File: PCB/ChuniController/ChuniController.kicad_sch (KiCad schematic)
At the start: 2 parts, among them U1 MPR121QR2_BOARD

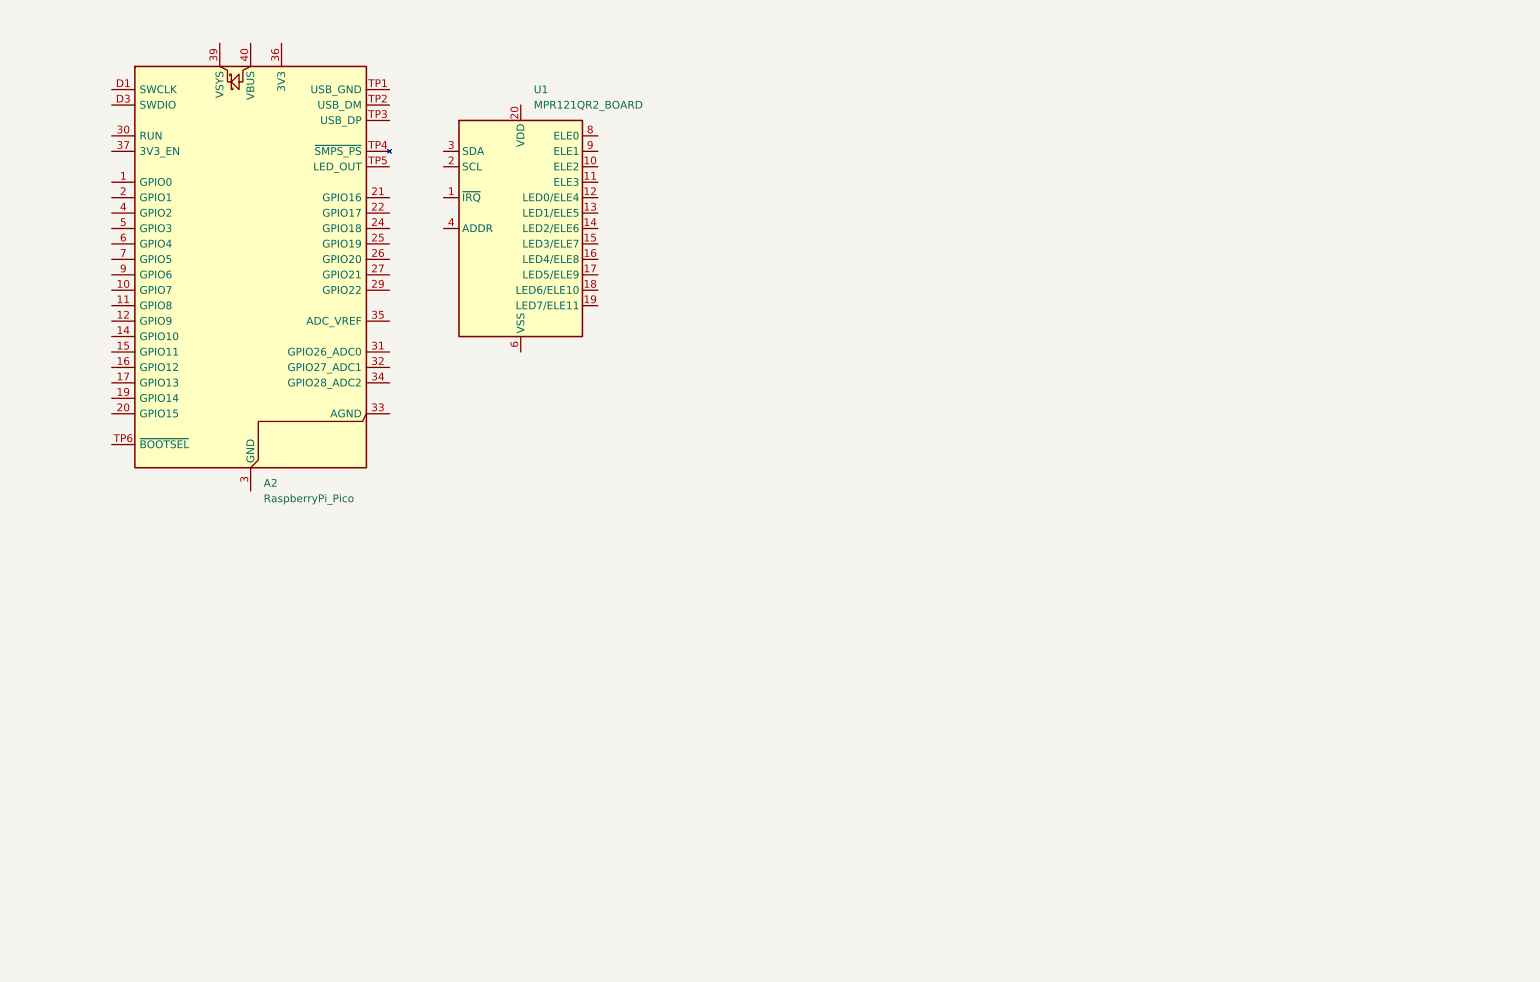
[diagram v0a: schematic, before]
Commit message: Add touch sensor
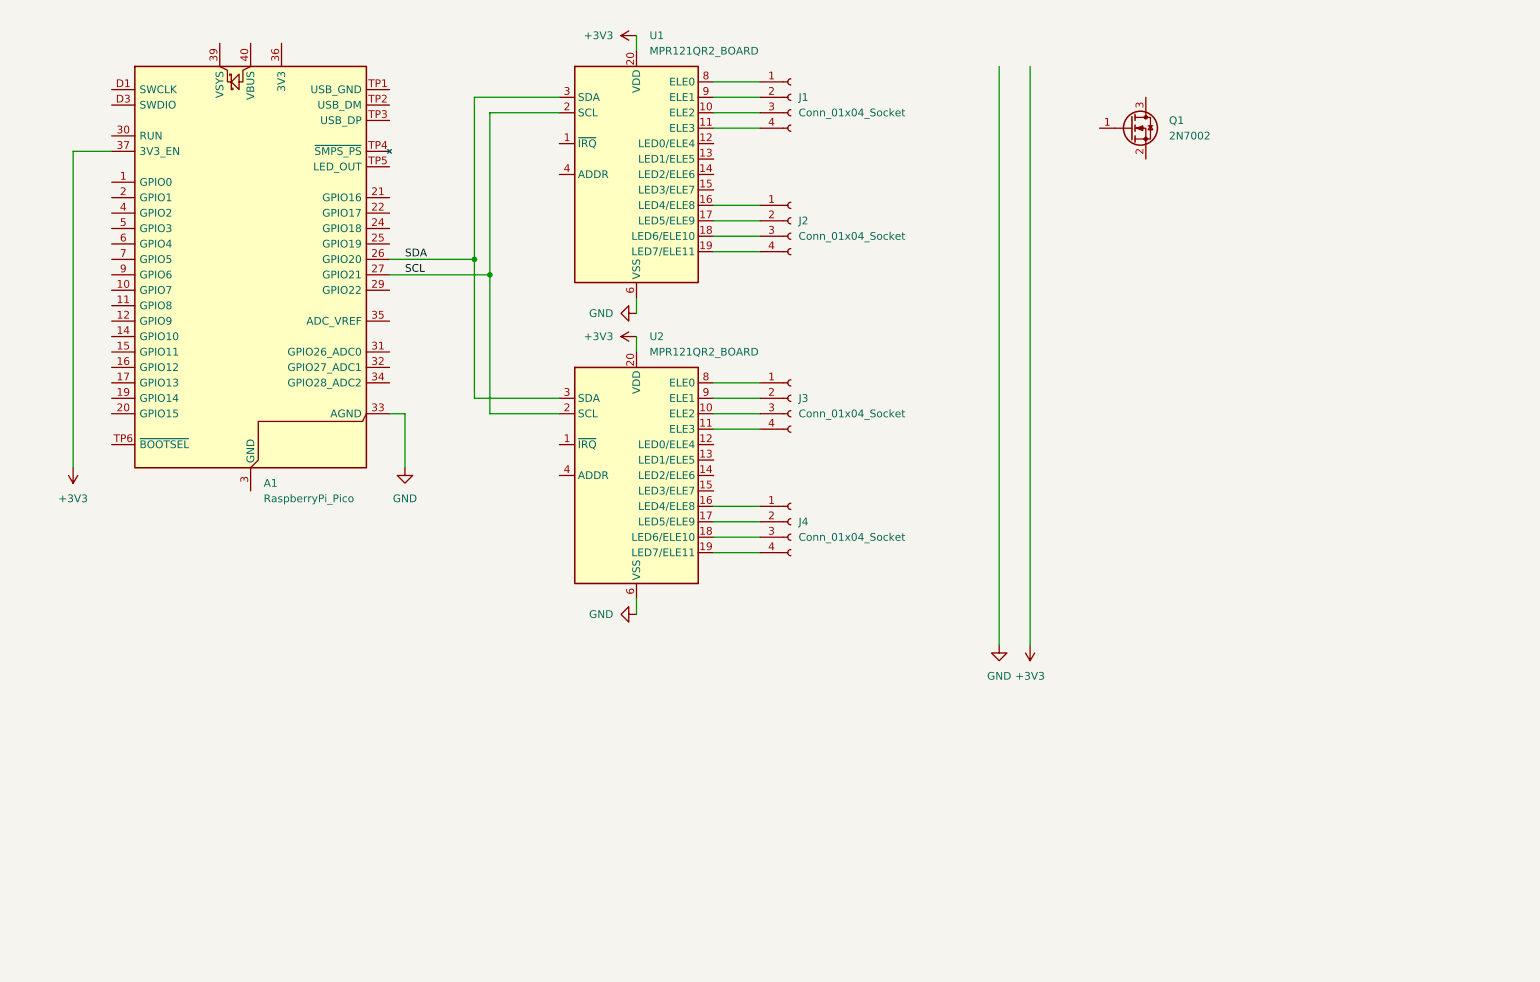
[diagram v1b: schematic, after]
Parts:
- added J1, J2, J3, J4: Conn_01x04_Socket, symbol Connector:Conn_01x04_Socket
- added Q1: 2N7002, Package_TO_SOT_SMD:SOT-23, symbol Transistor_FET:2N7002
- added U2: MPR121QR2_BOARD, chu_main:MPR121_BOARD, symbol 2025-07-05_08-37-47:MPR121QR2_BOARD
- renumbered A2 to A1
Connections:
- net SDA: now reaches A1.26 (GPIO20)
- net SDA: now also U1.3 (SDA), U2.3 (SDA)
- net SCL: now reaches A1.27 (GPIO21)
- net SCL: now also U1.2 (SCL), U2.2 (SCL)
- net GND: now reaches A1.33 (AGND)
- net GND: now also U1.6 (VSS), U2.6 (VSS)
- net +3V3: now reaches A1.37 (3V3_EN)
- net +3V3: now also U1.20 (VDD), U2.20 (VDD)
- net at U1.10 (ELE2): now also J1.3 (Pin_3)
- net at U1.11 (ELE3): now also J1.4 (Pin_4)
- net at U1.16 (LED4/ELE8): now also J2.1 (Pin_1)
- net at U1.17 (LED5/ELE9): now also J2.2 (Pin_2)
- net at U1.18 (LED6/ELE10): now also J2.3 (Pin_3)
- net at U1.19 (LED7/ELE11): now also J2.4 (Pin_4)
- net at U1.8 (ELE0): now also J1.1 (Pin_1)
- net at U1.9 (ELE1): now also J1.2 (Pin_2)
- new net: J4.1 (Pin_1), U2.16 (LED4/ELE8)
- new net: J4.2 (Pin_2), U2.17 (LED5/ELE9)
- new net: J4.3 (Pin_3), U2.18 (LED6/ELE10)
- new net: J4.4 (Pin_4), U2.19 (LED7/ELE11)
- new net: J3.3 (Pin_3), U2.10 (ELE2)
- new net: J3.4 (Pin_4), U2.11 (ELE3)
- new net: J3.1 (Pin_1), U2.8 (ELE0)
- new net: J3.2 (Pin_2), U2.9 (ELE1)
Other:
- moved on the sheet: U1

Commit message: Add IR sensor
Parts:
- added D1, D2, D3, D4, D5, D6: IR333C-A, LED_THT:LED_D5.0mm, symbol Device:LED
- added Q10, Q11, Q12, Q4, Q6: 2N7002, Package_TO_SOT_SMD:SOT-23, symbol Transistor_FET:2N7002
- added Q2, Q3, Q5, Q7, Q8, Q9: PT333-3B, OptoDevice:Kingbright_KPS-3227, symbol Sensor_Optical:BP103B
- added R1, R16, R17, R18, R6, R9: 1R, symbol Device:R
- added R10, R12, R14, R2, R4, R7: 10R, symbol Device:R
- added R11, R13, R15, R3, R5, R8: 10K, symbol Device:R
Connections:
- net +3V3: now also D1.2 (A), D2.2 (A), D3.2 (A), D4.2 (A), D5.2 (A), D6.2 (A), Q2.1 (C), Q3.1 (C), Q5.1 (C), Q7.1 (C), Q8.1 (C), Q9.1 (C)
- net GND: now also Q1.2 (S), Q10.2 (S), Q11.2 (S), Q12.2 (S), Q4.2 (S), Q6.2 (S), R11.1, R13.1, R15.1, R3.1, R5.1, R8.1
- net at Q1.1 (G): now also R2.2
- net at Q1.3 (D): now also R1.2
- new net: Q11.1 (G), R12.2
- new net: Q10.1 (G), R10.2
- new net: Q6.1 (G), R7.2
- new net: D1.1 (K), R1.1
- new net: D6.1 (K), R18.1
- new net: Q12.3 (D), R18.2
- new net: D3.1 (K), R9.1
- new net: D2.1 (K), R6.1
- new net: Q7.2 (E), R11.2
- new net: Q6.3 (D), R9.2
- new net: Q8.2 (E), R13.2
- new net: Q9.2 (E), R15.2
- new net: D4.1 (K), R16.1
- new net: Q11.3 (D), R17.2
- new net: Q10.3 (D), R16.2
- new net: Q5.2 (E), R8.2
- new net: Q2.2 (E), R3.2
- new net: Q4.1 (G), R4.2
- new net: Q3.2 (E), R5.2
- new net: Q4.3 (D), R6.2
- new net: Q12.1 (G), R14.2
- new net: D5.1 (K), R17.1
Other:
- moved on the sheet: Q1

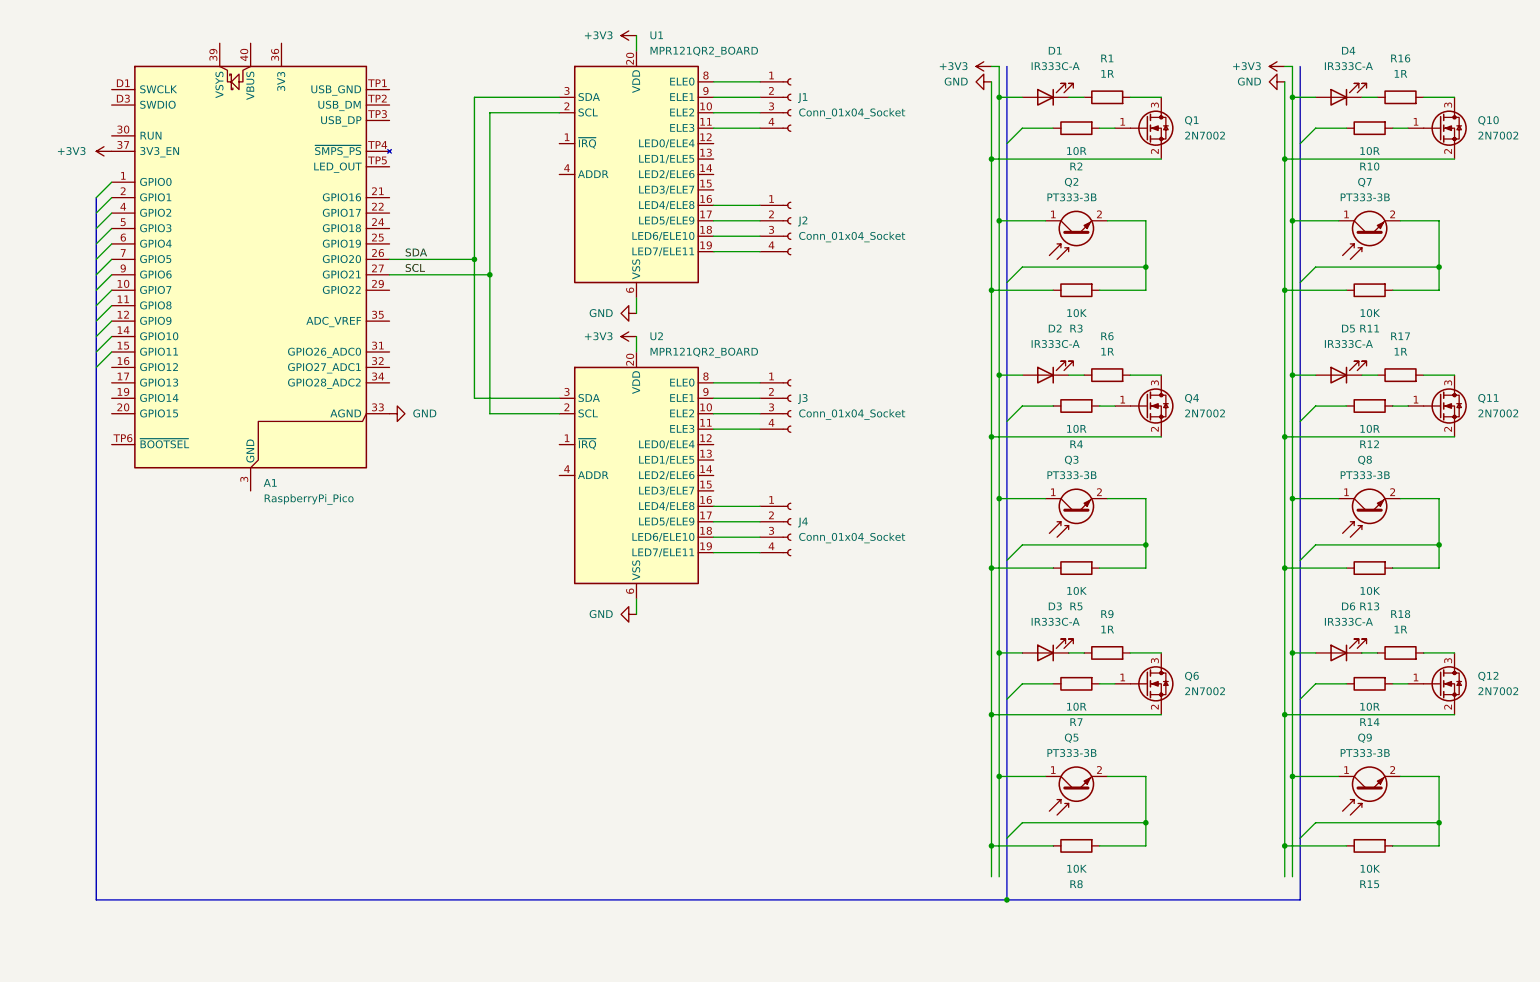
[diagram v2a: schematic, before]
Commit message: Seperate schematic to multiple page
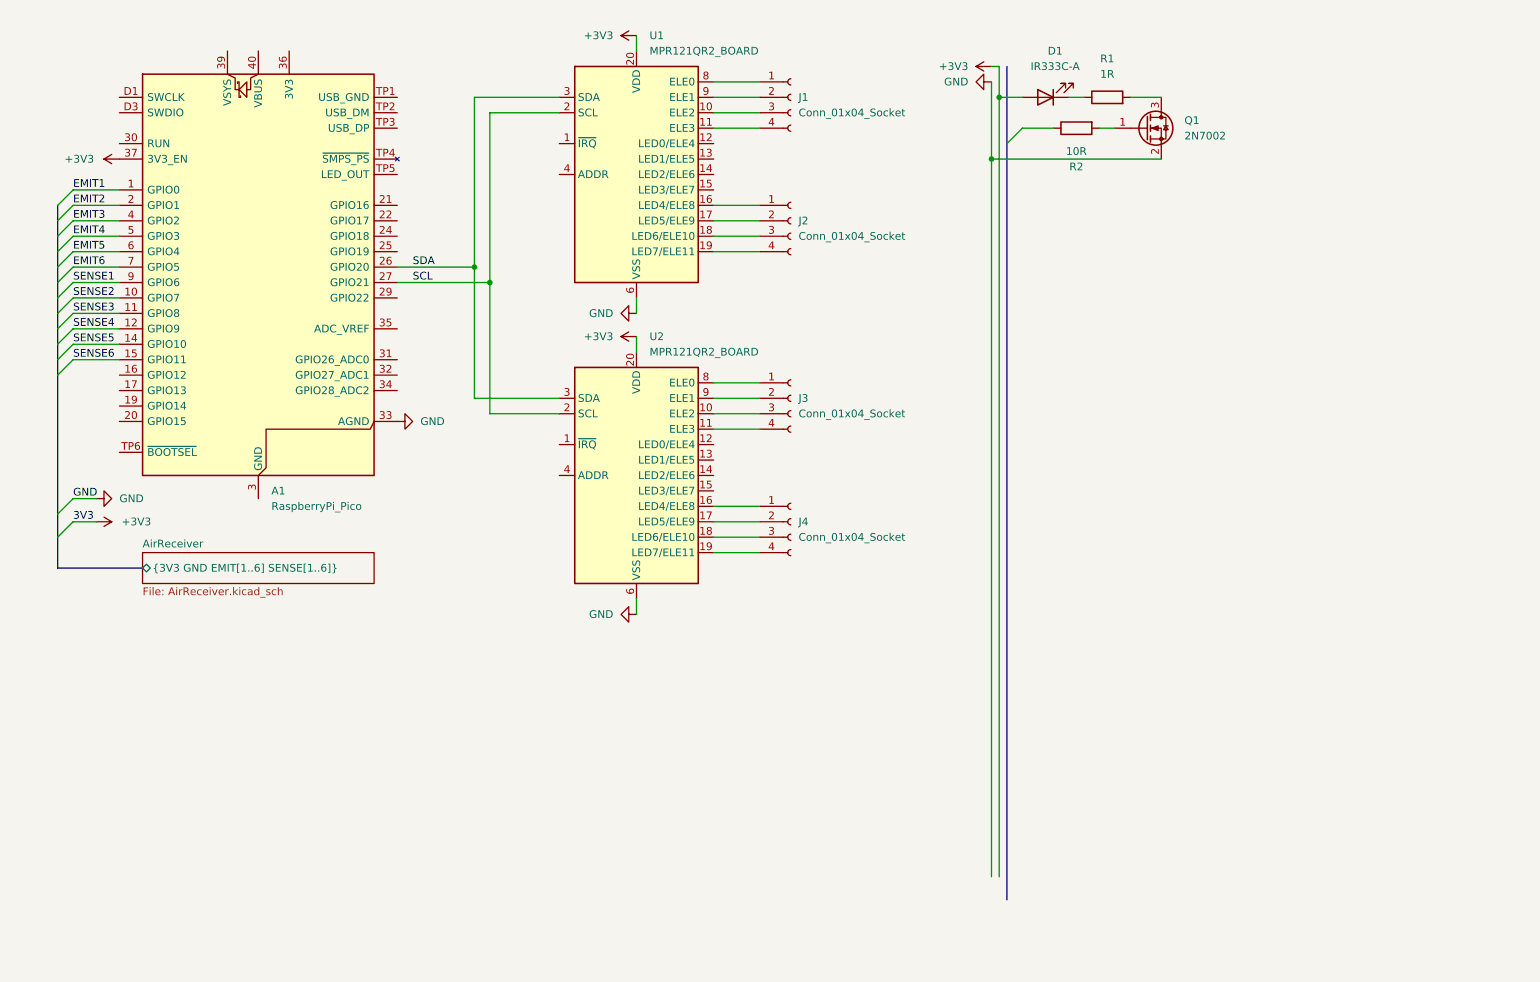
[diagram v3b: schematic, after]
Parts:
- removed D2, D3, D4, D5, D6: IR333C-A, LED_THT:LED_D5.0mm, symbol Device:LED
- removed Q10, Q11, Q12, Q4, Q6: 2N7002, Package_TO_SOT_SMD:SOT-23, symbol Transistor_FET:2N7002
- removed Q2, Q3, Q5, Q7, Q8, Q9: PT333-3B, OptoDevice:Kingbright_KPS-3227, symbol Sensor_Optical:BP103B
- removed R10, R12, R14, R4, R7: 10R, symbol Device:R
- removed R11, R13, R15, R3, R5, R8: 10K, symbol Device:R
- removed R16, R17, R18, R6, R9: 1R, symbol Device:R
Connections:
- net EMIT1: now reaches A1.1 (GPIO0)
- net SENSE2: now reaches A1.10 (GPIO7)
- net SENSE3: now reaches A1.11 (GPIO8)
- net SENSE4: now reaches A1.12 (GPIO9)
- net SENSE5: now reaches A1.14 (GPIO10)
- net SENSE6: now reaches A1.15 (GPIO11)
- net EMIT2: now reaches A1.2 (GPIO1)
- net EMIT3: now reaches A1.4 (GPIO2)
- net EMIT4: now reaches A1.5 (GPIO3)
- net EMIT5: now reaches A1.6 (GPIO4)
- net EMIT6: now reaches A1.7 (GPIO5)
- net SENSE1: now reaches A1.9 (GPIO6)
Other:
- added sheet AirReceiver (AirReceiver.kicad_sch)
- moved on the sheet: A1

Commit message: PCB + CAD
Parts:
- removed D1: IR333C-A, LED_THT:LED_D5.0mm, symbol Device:LED
- removed Q1: 2N7002, Package_TO_SOT_SMD:SOT-23, symbol Transistor_FET:2N7002
- removed R1: 1R, symbol Device:R
- removed R2: 10R, symbol Device:R
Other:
- added sheet AirBlaster (AirBlaster.kicad_sch)

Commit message: PCB
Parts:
- removed J1, J2, J3, J4: Conn_01x04_Socket, symbol Connector:Conn_01x04_Socket
- added J1, J2, J3, J4: Conn_01x04, symbol Connector_Generic:Conn_01x04
- added J5, J6, J7, J8: Conn_01x08, Connector_JST:JST_SH_SM08B-SRSS-TB_1x08-1MP_P1.00mm_Horizontal, symbol Connector_Generic:Conn_01x08
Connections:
- net +3V3: now also J5.1 (Pin_1)
- net EMIT1: now also J6.3 (Pin_3), J8.3 (Pin_3)
- net EMIT2: now also J6.4 (Pin_4), J8.4 (Pin_4)
- net EMIT3: now also J6.5 (Pin_5), J8.5 (Pin_5)
- net EMIT4: now also J6.6 (Pin_6), J8.6 (Pin_6)
- net EMIT5: now also J6.7 (Pin_7), J8.7 (Pin_7)
- net EMIT6: now also J6.8 (Pin_8), J8.8 (Pin_8)
- net GND: now also J5.2 (Pin_2), J6.2 (Pin_2)
- net SENSE1: now also J5.3 (Pin_3), J7.3 (Pin_3)
- net SENSE2: now also J5.4 (Pin_4), J7.4 (Pin_4)
- net SENSE3: now also J5.5 (Pin_5), J7.5 (Pin_5)
- net SENSE4: now also J5.6 (Pin_6), J7.6 (Pin_6)
- net SENSE5: now also J5.7 (Pin_7), J7.7 (Pin_7)
- net SENSE6: now also J5.8 (Pin_8), J7.8 (Pin_8)
- net +5V: now reaches A1.40 (VBUS)
- net +5V: now also J6.1 (Pin_1)
- net at U2.16 (LED4/ELE8): now also J4.1 (Pin_1)
- net at U2.17 (LED5/ELE9): now also J4.2 (Pin_2)
- net at U2.18 (LED6/ELE10): now also J4.3 (Pin_3)
- net at U2.19 (LED7/ELE11): now also J4.4 (Pin_4)
- net at U2.10 (ELE2): now also J3.3 (Pin_3)
- net at U2.11 (ELE3): now also J3.4 (Pin_4)
- net at U2.8 (ELE0): now also J3.1 (Pin_1)
- net at U2.9 (ELE1): now also J3.2 (Pin_2)
- net at U1.8 (ELE0): now also J1.1 (Pin_1)
- net at U1.9 (ELE1): now also J1.2 (Pin_2)
- net at U1.10 (ELE2): now also J1.3 (Pin_3)
- net at U1.11 (ELE3): now also J1.4 (Pin_4)
- net at U1.16 (LED4/ELE8): now also J2.1 (Pin_1)
- net at U1.17 (LED5/ELE9): now also J2.2 (Pin_2)
- net at U1.18 (LED6/ELE10): now also J2.3 (Pin_3)
- net at U1.19 (LED7/ELE11): now also J2.4 (Pin_4)
- new net AirBlaster/5V: J8.1 (Pin_1)
- new net AirBlaster/GND: J8.2 (Pin_2)
- new net AirReceiver/3V3: J7.1 (Pin_1)
- new net AirReceiver/GND: J7.2 (Pin_2)
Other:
- sheet AirBlaster ports: added 5V, GND, {EMIT[1..6]}; removed {3V3 GND EMIT[1..6] SENSE[1..6]}
- sheet AirReceiver ports: added 3V3, GND, {SENSE[1..6]}; removed {3V3 GND EMIT[1..6] SENSE[1..6]}

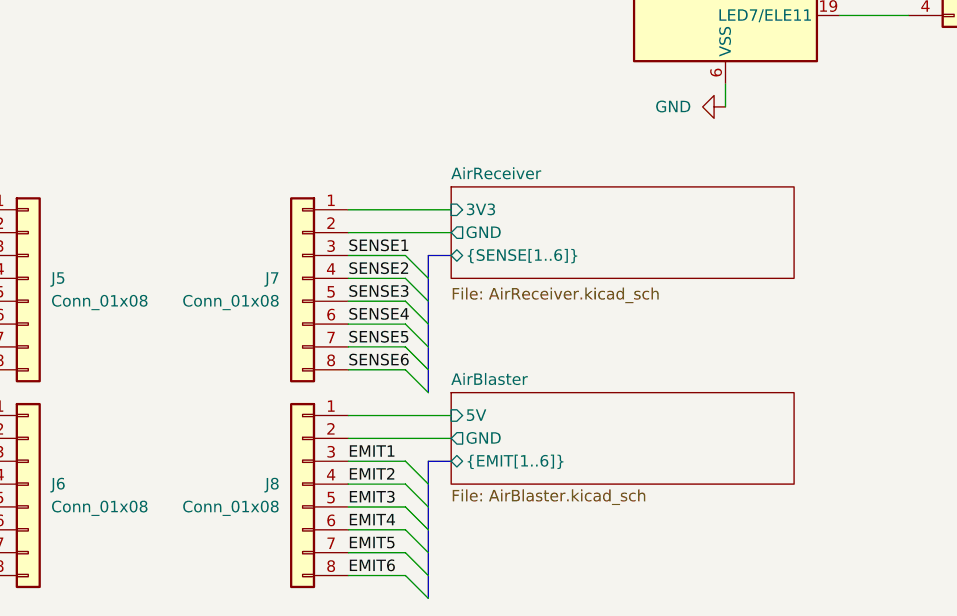
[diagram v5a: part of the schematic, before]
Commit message: PCB both ir board: ok add LM393D 3d model
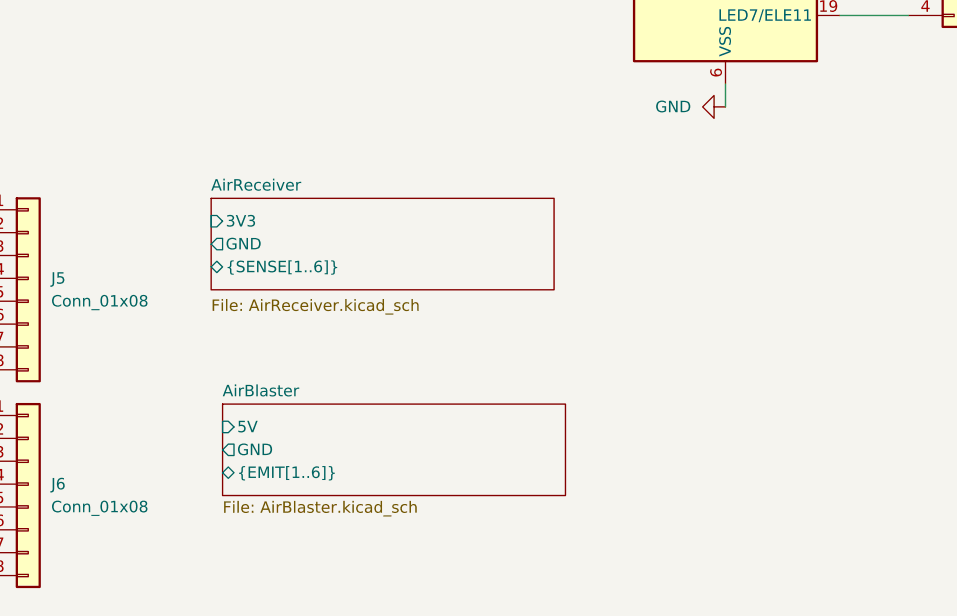
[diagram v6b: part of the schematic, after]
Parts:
- removed J7, J8: Conn_01x08, Connector_JST:JST_SH_SM08B-SRSS-TB_1x08-1MP_P1.00mm_Horizontal, symbol Connector_Generic:Conn_01x08
- J4: footprint (none) -> Connector_JST:JST_SH_SM04B-SRSS-TB_1x04-1MP_P1.00mm_Horizontal

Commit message: PCB
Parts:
- added J7, J8: Conn_01x08, Connector_JST:JST_SH_SM08B-SRSS-TB_1x08-1MP_P1.00mm_Horizontal, symbol Connector_Generic:Conn_01x08
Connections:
- net AirBlaster/5V: now also J8.1 (Pin_1)
- net AirBlaster/GND: now also J8.2 (Pin_2)
- net AirReceiver/3V3: now also J7.1 (Pin_1)
- net AirReceiver/GND: now also J7.2 (Pin_2)
- net EMIT1: now also J8.3 (Pin_3)
- net EMIT2: now also J8.4 (Pin_4)
- net EMIT3: now also J8.5 (Pin_5)
- net EMIT4: now also J8.6 (Pin_6)
- net EMIT5: now also J8.7 (Pin_7)
- net EMIT6: now also J8.8 (Pin_8)
- net SENSE1: now also J7.3 (Pin_3)
- net SENSE2: now also J7.4 (Pin_4)
- net SENSE3: now also J7.5 (Pin_5)
- net SENSE4: now also J7.6 (Pin_6)
- net SENSE5: now also J7.7 (Pin_7)
- net SENSE6: now also J7.8 (Pin_8)
